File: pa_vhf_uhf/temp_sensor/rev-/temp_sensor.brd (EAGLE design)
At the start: 160 x 100 mm, 0 parts

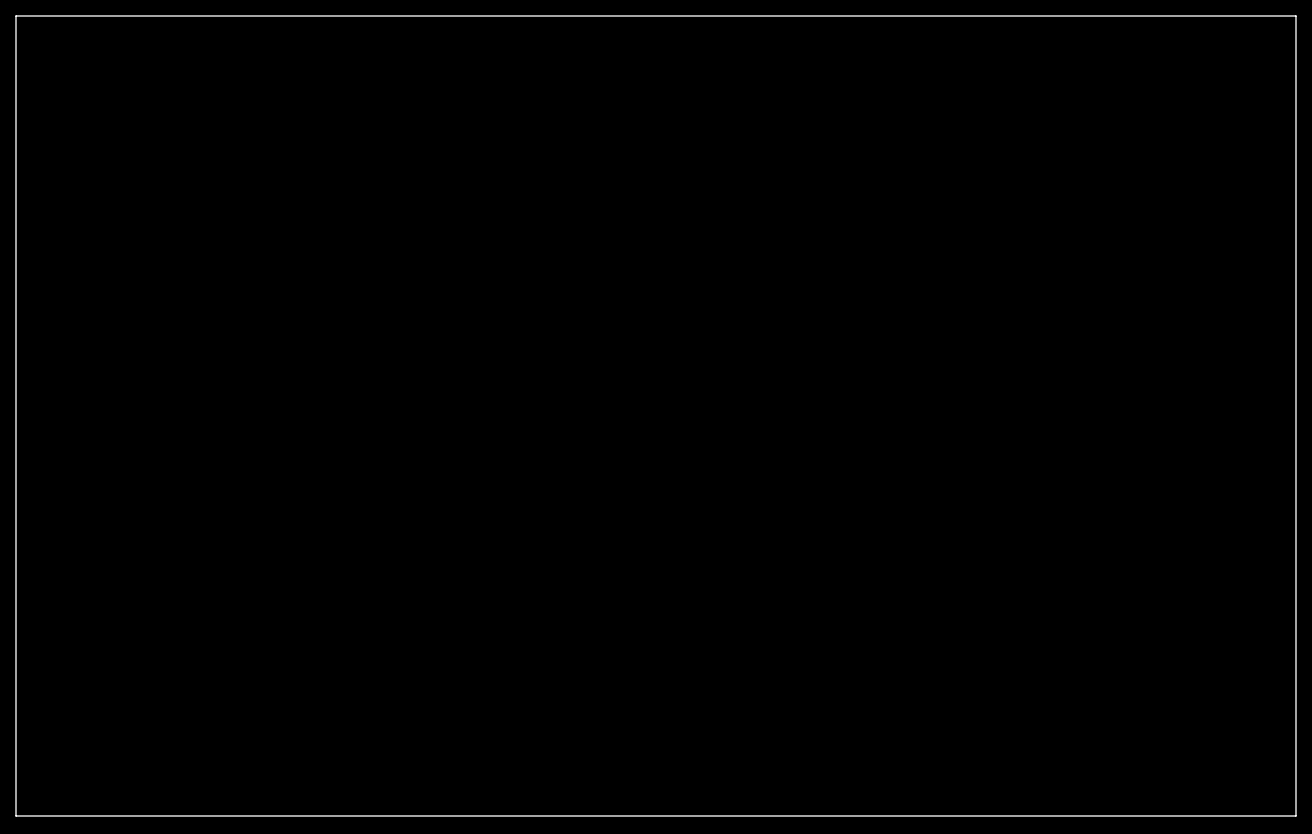
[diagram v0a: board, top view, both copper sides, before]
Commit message: final version of rev- for MCP9700 temp sensor for PA.
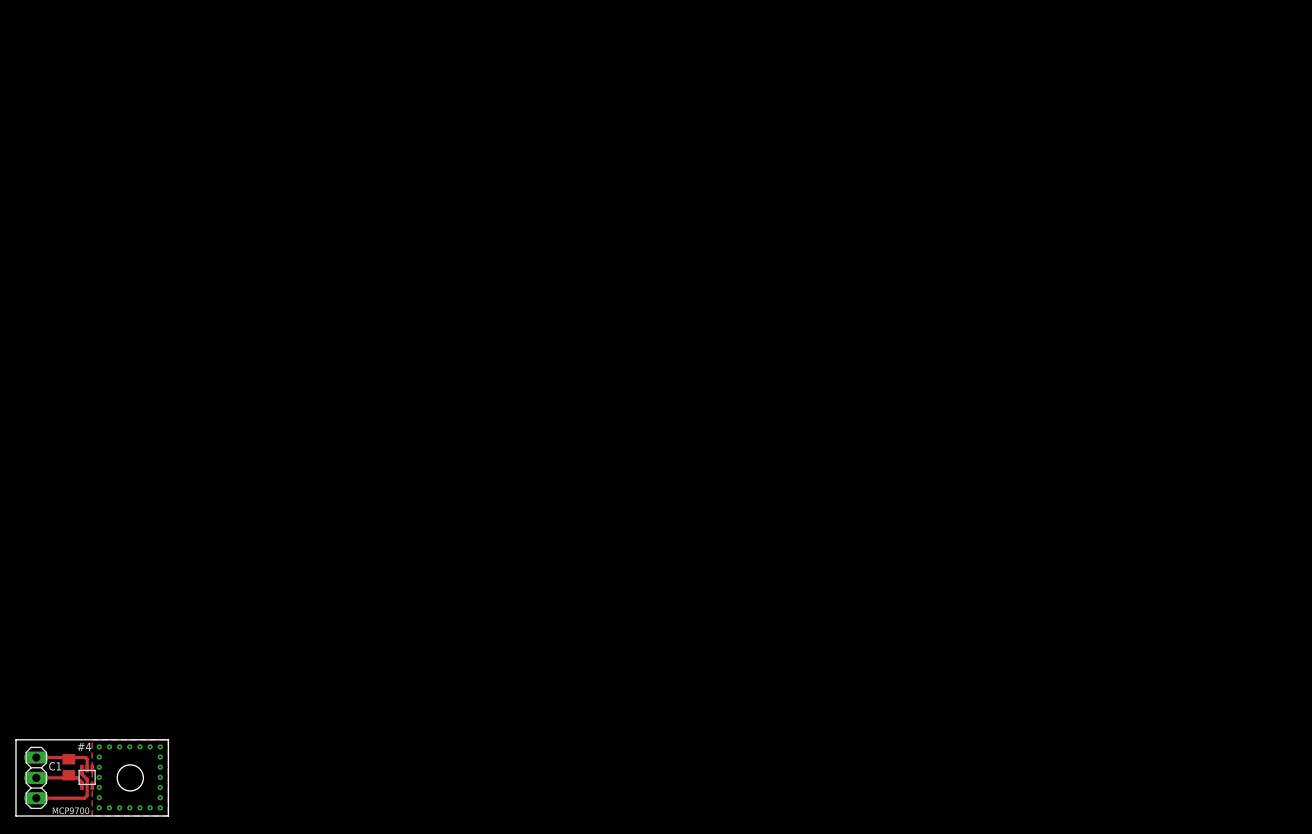
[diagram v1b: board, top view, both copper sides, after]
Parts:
- added C1: .1uF, rcl:C0805K
- added IC1: MCP9700, vtgs:SC70
- added JP1: (no value), pinhead:1X03
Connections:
- new net GND: C1.2, IC1.2, JP1.1
- new net THERM: IC1.1, IC1.5
- new net VDD: C1.1, IC1.4, JP1.2
- new net VOUT: IC1.3, JP1.3
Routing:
- net VOUT: track 0.00 -> 10.1 mm
- net GND: track 0.00 -> 7.82 mm
- net VDD: track 0.00 -> 6.74 mm
- added copper zone on layer 1, net THERM
- added copper zone on layer 16, net THERM
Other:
- board size 160 x 100 mm -> 19.1 x 9.5 mm
- board text added: "#4"
- board text added: "GND"
- board text added: "REV-"
- board text added: "VDD"
- board text added: "VOUT"
